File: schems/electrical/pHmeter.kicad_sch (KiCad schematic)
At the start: 30 parts, among them J1 Screw_Terminal_01x02, J2 Conn_01x04, J3 Conn_01x02, J4 Screw_Terminal_01x02, J5 SD_Card, J6 Conn_01x03_Pin, J7 Conn_01x03_Pin, J8 Screw_Terminal_01x03, J9 Screw_Terminal_01x03, K1 FINDER-36.11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

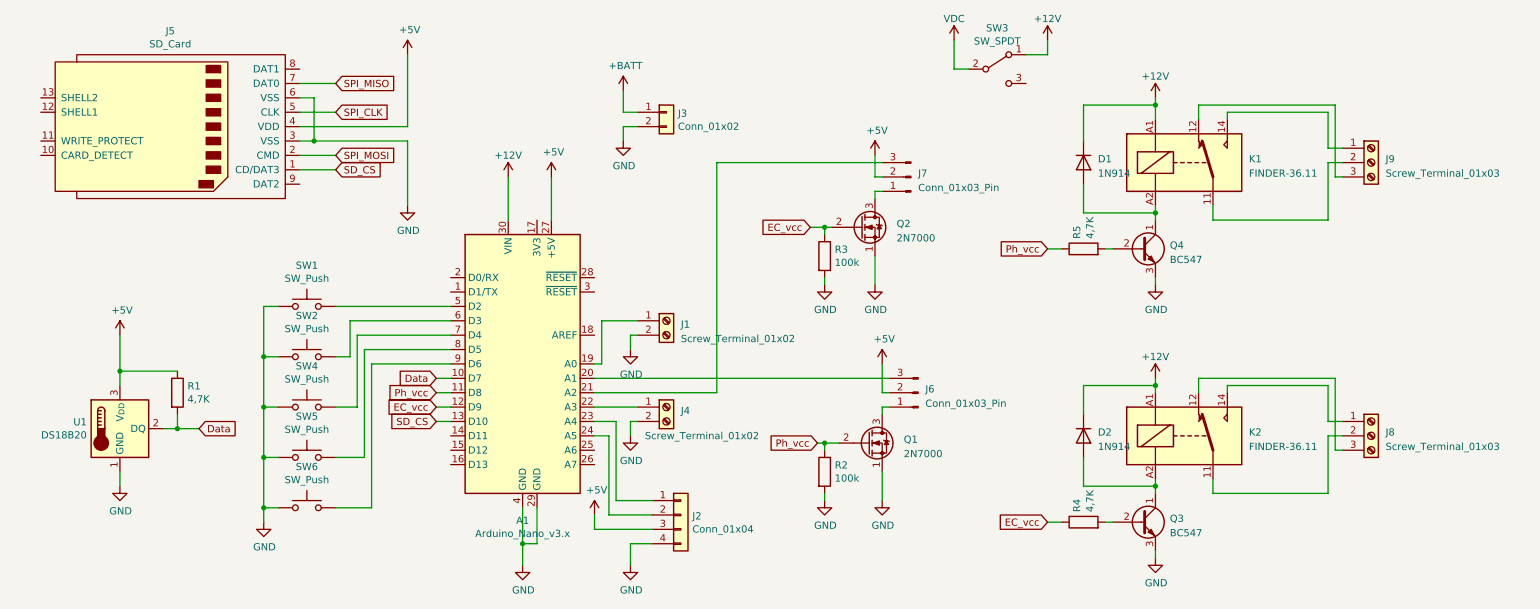
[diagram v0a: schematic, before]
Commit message: fix automation pins
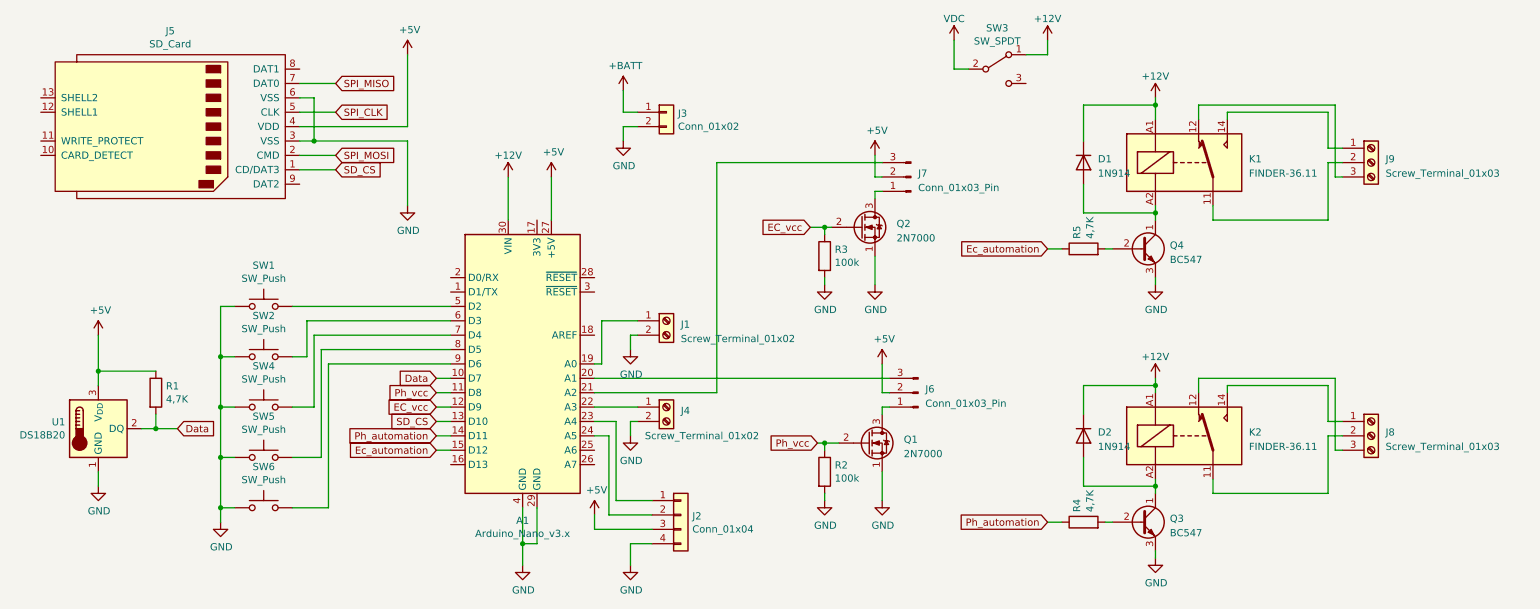
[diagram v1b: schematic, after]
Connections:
- net EC_vcc: no longer R4.1
- net Ph_vcc: no longer R5.1
- net Ph_automation: now reaches A1.14 (D11)
- net Ph_automation: now also R4.1
- net Ec_automation: now reaches A1.15 (D12)
- net Ec_automation: now also R5.1
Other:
- moved on the sheet: R1, SW1, SW2, SW4, SW5, SW6, U1
